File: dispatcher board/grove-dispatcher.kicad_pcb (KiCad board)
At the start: 2 copper layers, 156.8 x 75.6 mm, 75 parts, among them P1 CONN_01X12, P10 CONN_01X06, P11 CONN_01X06, P12 CONN_01X06, P13 CONN_01X06, P14 CONN_01X06, P15 CONN_01X06, P16 CONN_01X06, P17 CONN_01X06, P2 CONN_01X06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

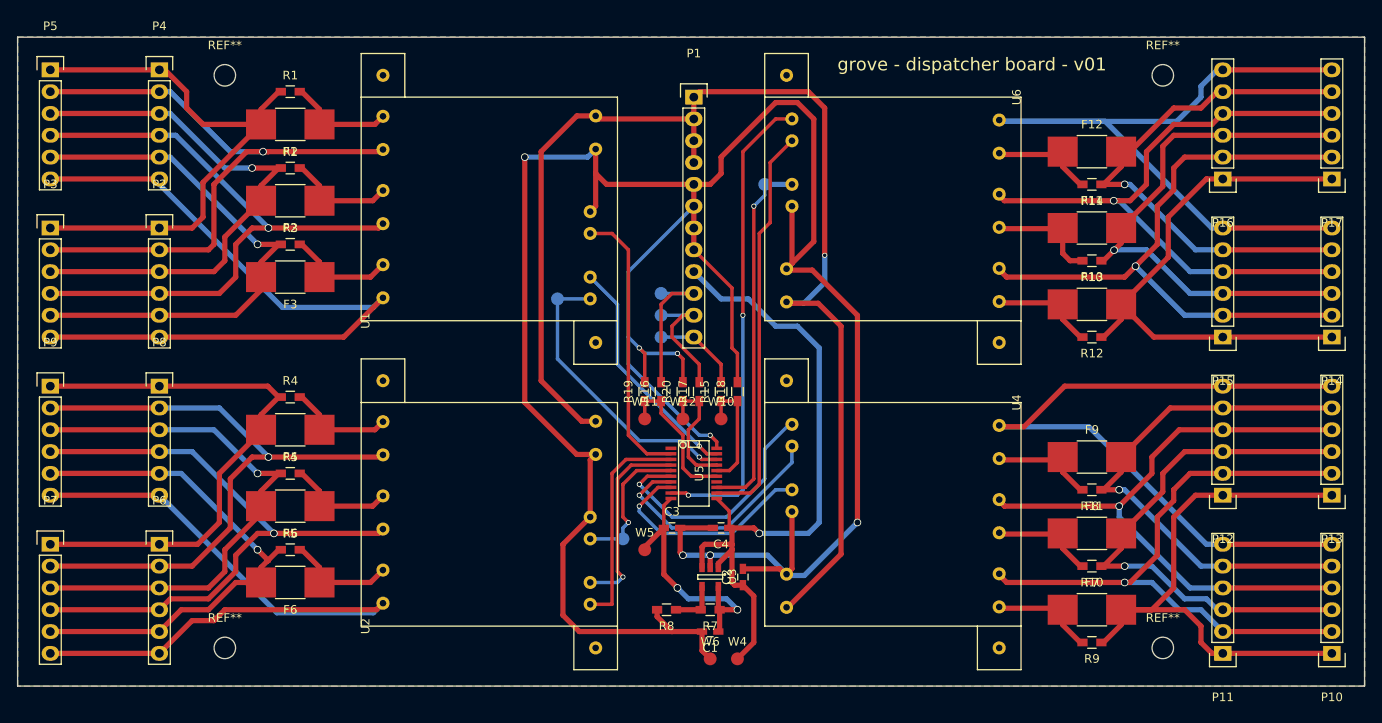
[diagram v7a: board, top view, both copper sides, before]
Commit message: Update silk screen
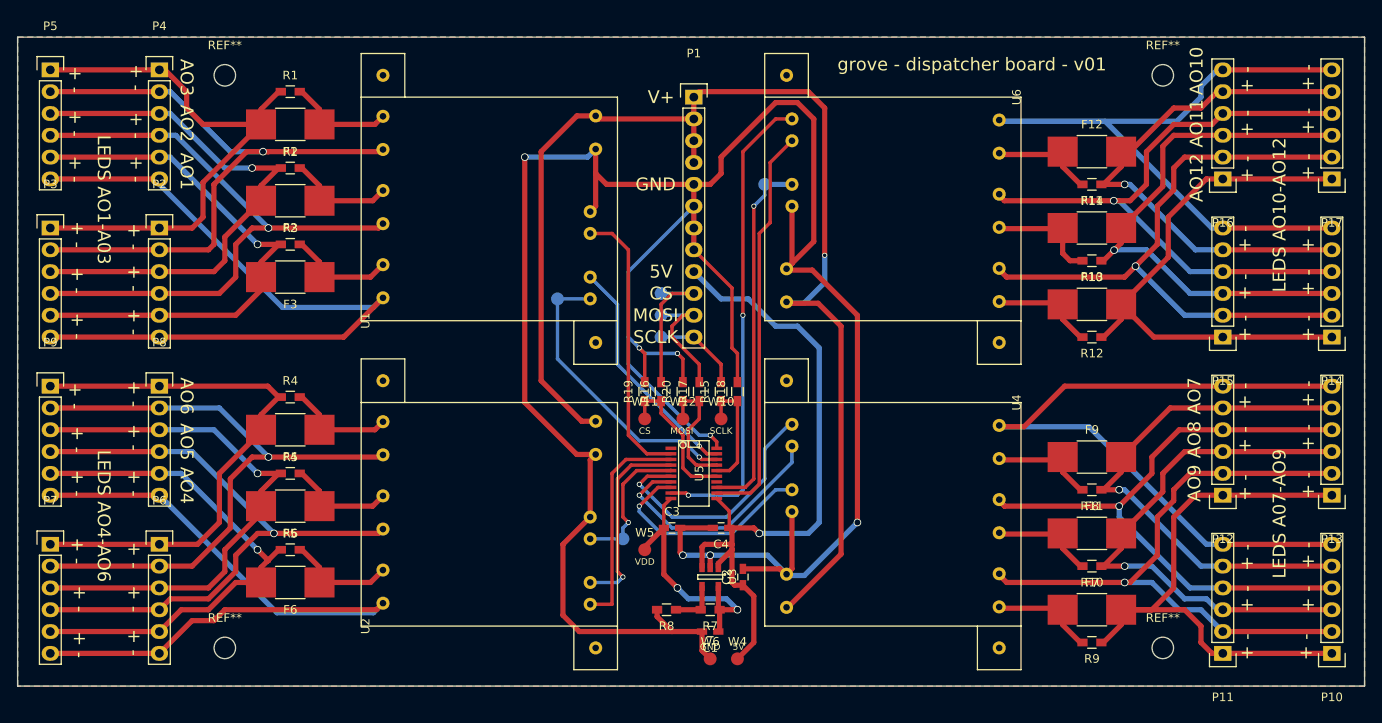
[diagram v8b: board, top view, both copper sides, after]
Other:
- board text added: "+ -"
- board text added: "5V"
- board text added: "AO1"
- board text added: "AO10"
- board text added: "AO11"
- board text added: "AO12"
- board text added: "AO2"
- board text added: "AO3"
- board text added: "AO4"
- board text added: "AO5"
- board text added: "AO6"
- board text added: "AO7"
- board text added: "AO8"
- board text added: "AO9"
- board text added: "CS"
- board text added: "GND"
- board text added: "LEDS A07-AO9"
- board text added: "LEDS AO1-A03"
- board text added: "LEDS AO10-AO12"
- board text added: "LEDS AO4-AO6"
- board text added: "MOSI"
- board text added: "SCLK"
- board text added: "V+"
- board text added: "VDD"
